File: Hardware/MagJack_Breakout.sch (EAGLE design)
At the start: 3 parts, among them J1 MAGJACK-NOLABELS

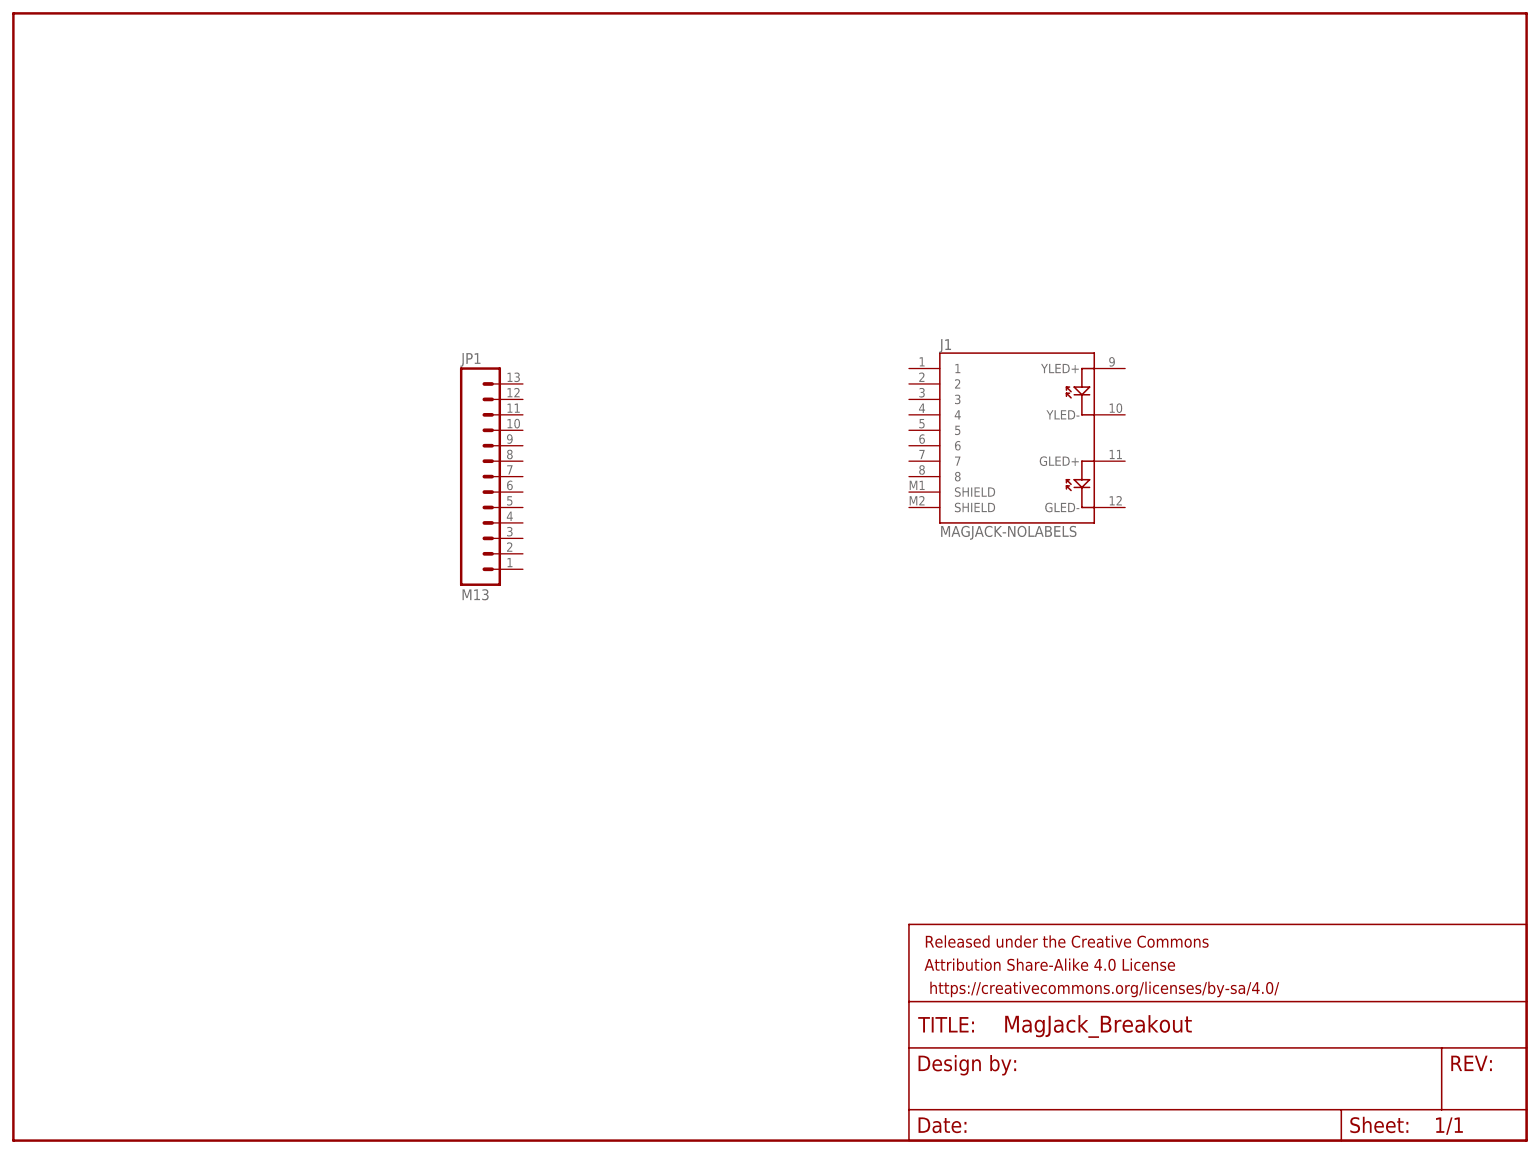
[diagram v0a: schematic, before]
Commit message: Completed revised layout for prototypes
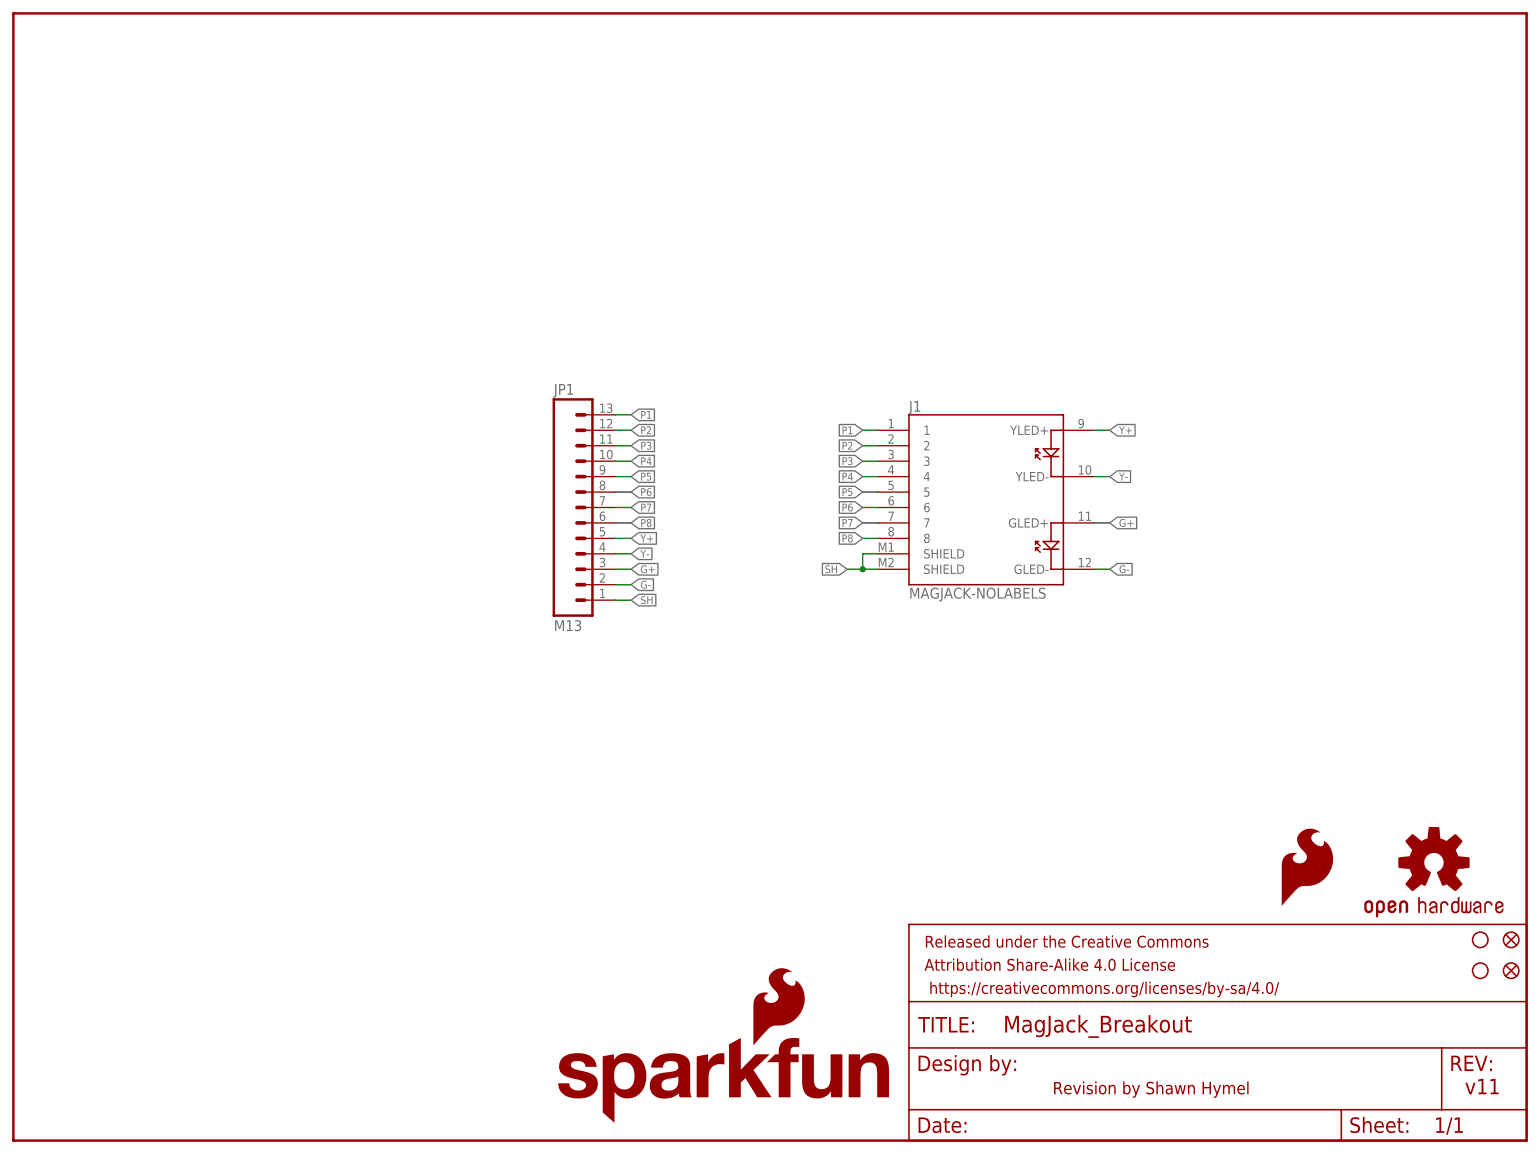
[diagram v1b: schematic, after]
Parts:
- added FID1, FID2: FIDUCIAL1X2, SparkFun-Aesthetics:FIDUCIAL1X2
- added LOGO1: OSHW-LOGOS, SparkFun-Aesthetics:OSHW-LOGOS
- added LOGO2: SFE_LOGO_FLAME.1_INCH, SparkFun-Aesthetics:SFE_LOGO_FLAME.1_INCH
- added LOGO3: SFE_LOGO_NAME_FLAME.1_INCH, SparkFun-Aesthetics:SFE_LOGO_NAME_FLAME.1_INCH
- added STANDOFF3, STANDOFF5: STAND-OFF, SparkFun-Electromechanical:STAND-OFF
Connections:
- new net G+: J1.GLED+, JP1.3
- new net G-: J1.GLED-, JP1.2
- new net P1: J1.1, JP1.13
- new net P2: J1.2, JP1.12
- new net P3: J1.3, JP1.11
- new net P4: J1.4, JP1.10
- new net P5: J1.5, JP1.9
- new net P6: J1.6, JP1.8
- new net P7: J1.7, JP1.7
- new net P8: J1.8, JP1.6
- new net SH: J1.SHIELD@0, J1.SHIELD@1, JP1.1
- new net Y+: J1.YLED+, JP1.5
- new net Y-: J1.YLED-, JP1.4
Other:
- note added: "Revision by Shawn Hymel"
- note added: "v11"
- moved on the sheet: J1, JP1
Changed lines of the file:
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@@
 <part name="JP1" library="SparkFun-Connectors" deviceset="M13" device=""/>
 <part name="J1" library="SparkFun-Connectors" deviceset="MAGJACK-NOLABELS" device=""/>
+<part name="FID1" library="SparkFun-Aesthetics" deviceset="FIDUCIAL" device="1X2"/>
+<part name="FID2" library="SparkFun-Aesthetics" deviceset="FIDUCIAL" device="1X2"/>
+<part name="STANDOFF3" library="SparkFun-Electromechanical" deviceset="STAND-OFF" device=""/>
+<part name="STANDOFF5" library="SparkFun-Electromechanical" deviceset="STAND-OFF" device=""/>
+<part name="LOGO1" library="SparkFun-Aesthetics" deviceset="OSHW-LOGO" device="S"/>
+<part name="LOGO2" library="SparkFun-Aesthetics" deviceset="SFE_LOGO_FLAME" device=".1_INCH"/>
+<part name="LOGO3" library="SparkFun-Aesthetics" deviceset="SFE_LOGO_NAME_FLAME" device=".1_INCH"/>
 </parts>
 <sheets>
 <sheet>
 <plain>
+<text x="170.942" y="7.62" size="2.032" layer="94">Revision by Shawn Hymel</text>
+<text x="238.76" y="7.62" size="2.54" layer="94">v11</text>
 </plain>
 <instances>
 <instance part="FRAME1" gate="G$1" x="0" y="0"/>
 <instance part="FRAME1" gate="G$2" x="147.32" y="0"/>
-<instance part="JP1" gate="G$1" x="73.66" y="109.22"/>
-<instance part="J1" gate="G$1" x="165.1" y="116.84"/>
+<instance part="JP1" gate="G$1" x="88.9" y="104.14"/>
+<instance part="J1" gate="G$1" x="160.02" y="106.68"/>
+<instance part="FID1" gate="G$1" x="246.38" y="27.94"/>
+<instance part="FID2" gate="G$1" x="246.38" y="33.02"/>
+<instance part="STANDOFF3" gate="G$1" x="241.3" y="33.02"/>
+<instance part="STANDOFF5" gate="G$1" x="241.3" y="27.94"/>
+<instance part="LOGO1" gate="G$1" x="233.68" y="45.72"/>
+<instance part="LOGO2" gate="G$1" x="208.28" y="38.1"/>
+<instance part="LOGO3" gate="G$1" x="88.9" y="2.54"/>
 </instances>
 <busses>
 </busses>
 <nets>
+<net name="P1" class="0">
+<segment>
+<pinref part="J1" gate="G$1" pin="1"/>
+<wire x1="142.24" y1="116.84" x2="139.7" y2="116.84" width="0.1524" layer="91"/>
+<label x="139.7" y="116.84" size="1.27" layer="95" rot="R180" xref="yes"/>
+</segment>
+<segment>
+<pinref part="JP1" gate="G$1" pin="13"/>
+<wire x1="99.06" y1="119.38" x2="101.6" y2="119.38" width="0.1524" layer="91"/>
+<label x="101.6" y="119.38" size="1.27" layer="95" xref="yes"/>
+</segment>
+</net>
+<net name="P2" class="0">
+<segment>
+<pinref part="J1" gate="G$1" pin="2"/>
+<wire x1="142.24" y1="114.3" x2="139.7" y2="114.3" width="0.1524" layer="91"/>
+<label x="139.7" y="114.3" size="1.27" layer="95" rot="R180" xref="yes"/>
+</segment>
+<segment>
+<pinref part="JP1" gate="G$1" pin="12"/>
+<wire x1="99.06" y1="116.84" x2="101.6" y2="116.84" width="0.1524" layer="91"/>
+<label x="101.6" y="116.84" size="1.27" layer="95" xref="yes"/>
+</segment>
+</net>
+<net name="P3" class="0">
+<segment>
+<pinref part="J1" gate="G$1" pin="3"/>
+<wire x1="142.24" y1="111.76" x2="139.7" y2="111.76" width="0.1524" layer="91"/>
+<label x="139.7" y="111.76" size="1.27" layer="95" rot="R180" xref="yes"/>
+</segment>
+<segment>
+<pinref part="JP1" gate="G$1" pin="11"/>
+<wire x1="101.6" y1="114.3" x2="99.06" y2="114.3" width="0.1524" layer="91"/>
+<label x="101.6" y="114.3" size="1.27" layer="95" xref="yes"/>
+</segment>
+</net>
+<net name="P4" class="0">
+<segment>
+<pinref part="J1" gate="G$1" pin="4"/>
+<wire x1="142.24" y1="109.22" x2="139.7" y2="109.22" width="0.1524" layer="91"/>
+<label x="139.7" y="109.22" size="1.27" layer="95" rot="R180" xref="yes"/>
+</segment>
+<segment>
+<pinref part="JP1" gate="G$1" pin="10"/>
+<wire x1="101.6" y1="111.76" x2="99.06" y2="111.76" width="0.1524" layer="91"/>
+<label x="101.6" y="111.76" size="1.27" layer="95" xref="yes"/>
+</segment>
+</net>
+<net name="P5" class="0">
+<segment>
+<pinref part="J1" gate="G$1" pin="5"/>
+<wire x1="142.24" y1="106.68" x2="139.7" y2="106.68" width="0.1524" layer="91"/>
+<label x="139.7" y="106.68" size="1.27" layer="95" rot="R180" xref="yes"/>
+</segment>
+<segment>
+<pinref part="JP1" gate="G$1" pin="9"/>
+<wire x1="101.6" y1="109.22" x2="99.06" y2="109.22" width="0.1524" layer="91"/>
+<label x="101.6" y="109.22" size="1.27" layer="95" xref="yes"/>
+</segment>
+</net>
+<net name="P6" class="0">
+<segment>
+<pinref part="J1" gate="G$1" pin="6"/>
+<wire x1="142.24" y1="104.14" x2="139.7" y2="104.14" width="0.1524" layer="91"/>
+<label x="139.7" y="104.14" size="1.27" layer="95" rot="R180" xref="yes"/>
+</segment>
+<segment>
+<pinref part="JP1" gate="G$1" pin="8"/>
+<wire x1="101.6" y1="106.68" x2="99.06" y2="106.68" width="0.1524" layer="91"/>
+<label x="101.6" y="106.68" size="1.27" layer="95" xref="yes"/>
+</segment>
+</net>
+<net name="P7" class="0">
+<segment>
+<pinref part="J1" gate="G$1" pin="7"/>
+<wire x1="142.24" y1="101.6" x2="139.7" y2="101.6" width="0.1524" layer="91"/>
+<label x="139.7" y="101.6" size="1.27" layer="95" rot="R180" xref="yes"/>
+</segment>
+<segment>
+<pinref part="JP1" gate="G$1" pin="7"/>
+<wire x1="101.6" y1="104.14" x2="99.06" y2="104.14" width="0.1524" layer="91"/>
+<label x="101.6" y="104.14" size="1.27" layer="95" xref="yes"/>
+</segment>
+</net>
+<net name="P8" class="0">
+<segment>
+<pinref part="J1" gate="G$1" pin="8"/>
+<wire x1="142.24" y1="99.06" x2="139.7" y2="99.06" width="0.1524" layer="91"/>
+<label x="139.7" y="99.06" size="1.27" layer="95" rot="R180" xref="yes"/>
+</segment>
+<segment>
+<pinref part="JP1" gate="G$1" pin="6"/>
+<wire x1="99.06" y1="101.6" x2="101.6" y2="101.6" width="0.1524" layer="91"/>
+<label x="101.6" y="101.6" size="1.27" layer="95" xref="yes"/>
+</segment>
+</net>
+<net name="SH" class="0">
+<segment>
+<pinref part="J1" gate="G$1" pin="SHIELD@0"/>
+<wire x1="142.24" y1="96.52" x2="139.7" y2="96.52" width="0.1524" layer="91"/>
+<pinref part="J1" gate="G$1" pin="SHIELD@1"/>
+<wire x1="142.24" y1="93.98" x2="139.7" y2="93.98" width="0.1524" layer="91"/>
+<wire x1="139.7" y1="96.52" x2="139.7" y2="93.98" width="0.1524" layer="91"/>
+<wire x1="139.7" y1="93.98" x2="137.16" y2="93.98" width="0.1524" layer="91"/>
+<junction x="139.7" y="93.98"/>
+<label x="137.16" y="93.98" size="1.27" layer="95" rot="R180" xref="yes"/>
+</segment>
+<segment>
+<pinref part="JP1" gate="G$1" pin="1"/>
+<wire x1="99.06" y1="88.9" x2="101.6" y2="88.9" width="0.1524" layer="91"/>
+<label x="101.6" y="88.9" size="1.27" layer="95" xref="yes"/>
+</segment>
+</net>
+<net name="Y+" class="0">
+<segment>
+<pinref part="J1" gate="G$1" pin="YLED+"/>
+<wire x1="177.8" y1="116.84" x2="180.34" y2="116.84" width="0.1524" layer="91"/>
+<label x="180.34" y="116.84" size="1.27" layer="95" xref="yes"/>
+</segment>
+<segment>
+<pinref part="JP1" gate="G$1" pin="5"/>
+<wire x1="99.06" y1="99.06" x2="101.6" y2="99.06" width="0.1524" layer="91"/>
+<label x="101.6" y="99.06" size="1.27" layer="95" xref="yes"/>
+</segment>
+</net>
+<net name="Y-" class="0">
+<segment>
+<pinref part="J1" gate="G$1" pin="YLED-"/>
+<wire x1="177.8" y1="109.22" x2="180.34" y2="109.22" width="0.1524" layer="91"/>
+<label x="180.34" y="109.22" size="1.27" layer="95" xref="yes"/>
+</segment>
+<segment>
+<pinref part="JP1" gate="G$1" pin="4"/>
+<wire x1="99.06" y1="96.52" x2="101.6" y2="96.52" width="0.1524" layer="91"/>
+<label x="101.6" y="96.52" size="1.27" layer="95" xref="yes"/>
+</segment>
+</net>
+<net name="G+" class="0">
+<segment>
+<pinref part="J1" gate="G$1" pin="GLED+"/>
+<wire x1="177.8" y1="101.6" x2="180.34" y2="101.6" width="0.1524" layer="91"/>
+<label x="180.34" y="101.6" size="1.27" layer="95" xref="yes"/>
+</segment>
+<segment>
+<pinref part="JP1" gate="G$1" pin="3"/>
+<wire x1="101.6" y1="93.98" x2="99.06" y2="93.98" width="0.1524" layer="91"/>
+<label x="101.6" y="93.98" size="1.27" layer="95" xref="yes"/>
+</segment>
+</net>
+<net name="G-" class="0">
+<segment>
+<pinref part="J1" gate="G$1" pin="GLED-"/>
+<wire x1="177.8" y1="93.98" x2="180.34" y2="93.98" width="0.1524" layer="91"/>
+<label x="180.34" y="93.98" size="1.27" layer="95" xref="yes"/>
+</segment>
+<segment>
+<pinref part="JP1" gate="G$1" pin="2"/>
+<wire x1="101.6" y1="91.44" x2="99.06" y2="91.44" width="0.1524" layer="91"/>
+<label x="101.6" y="91.44" size="1.27" layer="95" xref="yes"/>
+</segment>
+</net>
 </nets>
 </sheet>

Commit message: Added Nate as original designer
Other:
- note added: "N. Seidle Revision by Shawn Hymel"
- note removed: "Revision by Shawn Hymel"
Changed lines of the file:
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@@
 <setting verticaltext="up"/>
 </settings>
-<grid distance="0.1" unitdist="inch" unit="inch" style="lines" multiple="1" display="yes" altdistance="0.01" altunitdist="inch" altunit="inch"/>
+<grid distance="0.1" unitdist="inch" unit="inch" style="lines" multiple="1" display="no" altdistance="0.01" altunitdist="inch" altunit="inch"/>
 <layers>
 <layer number="1" name="Top" color="4" fill="1" visible="no" active="no"/>
@@
 <sheet>
 <plain>
-<text x="170.942" y="7.62" size="2.032" layer="94">Revision by Shawn Hymel</text>
+<text x="170.942" y="7.62" size="2.032" layer="94">N. Seidle
+Revision by Shawn Hymel</text>
 <text x="238.76" y="7.62" size="2.54" layer="94">v11</text>
 </plain>
@@
 </schematic>
 </drawing>
+<compatibility>
+<note version="6.3" minversion="6.2.2" severity="warning">
+Since Version 6.2.2 text objects can contain more than one line,
+which will not be processed correctly with this version.
+</note>
+</compatibility>
 </eagle>

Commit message: Moved bottom/header section down by 0.1 in,
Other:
- note added: "v12"
- note removed: "v11"
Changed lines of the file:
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@@
 <text x="170.942" y="7.62" size="2.032" layer="94">N. Seidle
 Revision by Shawn Hymel</text>
-<text x="238.76" y="7.62" size="2.54" layer="94">v11</text>
+<text x="238.76" y="7.62" size="2.54" layer="94">v12</text>
 </plain>
 <instances>

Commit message: Added locking header
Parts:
- JP1: value M13 -> M13LOCK; device SparkFun-Connectors:M13 -> SparkFun-Connectors:M13LOCK
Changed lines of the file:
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@@
 <parts>
 <part name="FRAME1" library="SparkFun-Aesthetics" deviceset="FRAME-LETTER" device=""/>
-<part name="JP1" library="SparkFun-Connectors" deviceset="M13" device=""/>
+<part name="JP1" library="SparkFun-Connectors" deviceset="M13" device="LOCK" value="M13LOCK"/>
 <part name="J1" library="SparkFun-Connectors" deviceset="MAGJACK-NOLABELS" device=""/>
 <part name="FID1" library="SparkFun-Aesthetics" deviceset="FIDUCIAL" device="1X2"/>
